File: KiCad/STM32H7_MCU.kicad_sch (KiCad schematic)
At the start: 51 parts, among them IC2 SN74LVC1G14DBVR, IC3 STM32H7R7L8H6H, IC4 TLV75718PDRVR, Y1 VXM7-9032-25M0000000

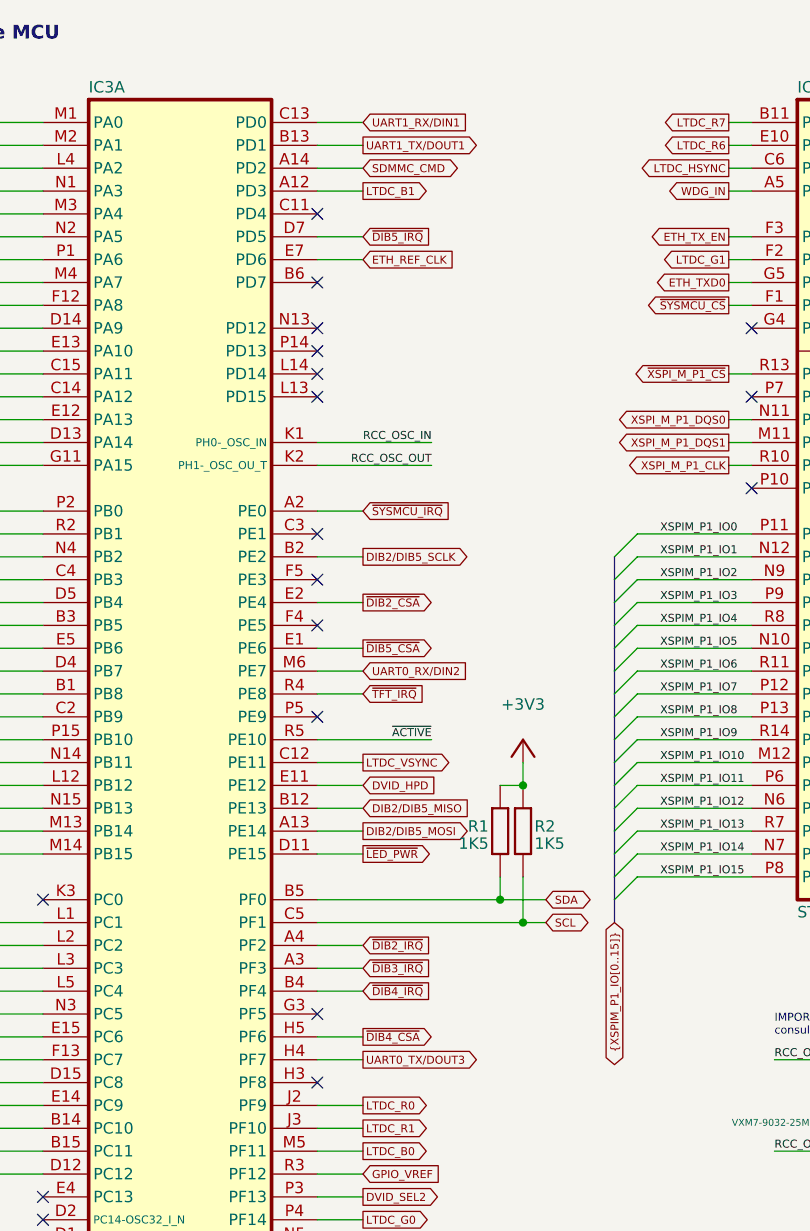
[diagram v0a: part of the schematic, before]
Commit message: DIN3 pin assigned
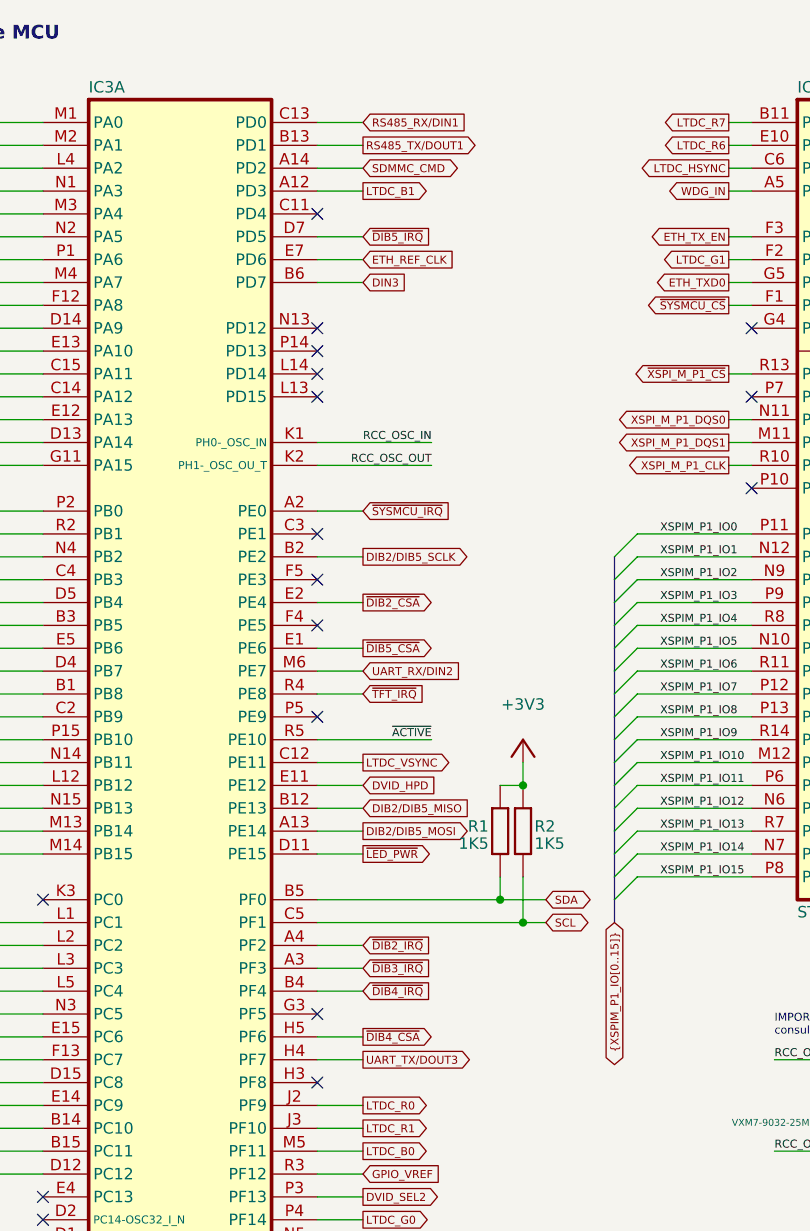
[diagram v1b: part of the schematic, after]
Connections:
- net DIN3: now reaches IC3.B6 (PD7)
- net UART0_RX/DIN2 renamed UART_RX/DIN2
- net UART0_TX/DOUT3 renamed UART_TX/DOUT3
- net UART1_RX/DIN1 renamed RS485_RX/DIN1
- net UART1_TX/DOUT1 renamed RS485_TX/DOUT1
- no-connect marks 27 -> 26
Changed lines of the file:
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@@
 	(title_block
 		(title "${project_name}")
-		(date "2025-11-17")
+		(date "2025-11-23")
 		(rev "${project_version}")
 		(company "${project_creator}")
@@
 	)
 	(no_connect
-		(at 71.12 45.72)
-	)
-	(no_connect
 		(at 71.12 38.1)
 	)
@@
 	(wire
 		(pts
+			(xy 76.2 45.72) (xy 71.12 45.72)
+		)
+		(stroke
+			(width 0)
+			(type default)
+		)
+	)
+	(wire
+		(pts
 			(xy 149.86 137.16) (xy 149.86 139.7)
 		)
@@
 		)
 	)
-	(global_label "UART0_RX{slash}DIN2"
+	(global_label "UART_RX{slash}DIN2"
 		(shape input)
 		(at 76.2 88.9 0)
@@
 		)
 		(property "Intersheetrefs" "${INTERSHEET_REFS}"
-			(at 88.3725 88.9 0)
+			(at 87.5258 88.9 0)
 			(effects
 				(font
@@
 		)
 	)
-	(global_label "UART1_RX{slash}DIN1"
+	(global_label "RS485_RX{slash}DIN1"
 		(shape input)
 		(at 76.2 27.94 0)
@@
 		)
 		(property "Intersheetrefs" "${INTERSHEET_REFS}"
-			(at 88.3725 27.94 0)
+			(at 88.542 27.94 0)
 			(effects
 				(font
@@
 		)
 	)
-	(global_label "UART0_TX{slash}DOUT3"
+	(global_label "UART_TX{slash}DOUT3"
 		(shape output)
 		(at 76.2 132.08 0)
@@
 		)
 		(property "Intersheetrefs" "${INTERSHEET_REFS}"
-			(at 89.3461 132.08 0)
+			(at 88.4994 132.08 0)
 			(effects
 				(font
@@
 		)
 	)
-	(global_label "UART1_TX{slash}DOUT1"
+	(global_label "RS485_TX{slash}DOUT1"
 		(shape output)
 		(at 76.2 30.48 0)
@@
 		)
 		(property "Intersheetrefs" "${INTERSHEET_REFS}"
-			(at 89.3461 30.48 0)
+			(at 89.5156 30.48 0)
 			(effects
 				(font
@@
 				(hide yes)
 			)
+		)
+	)
+	(global_label "DIN3"
+		(shape input)
+		(at 76.2 45.72 0)
+		(fields_autoplaced yes)
+		(effects
+			(font
+				(size 0.889 0.889)
+			)
+			(justify left)
+		)
+		(property "Intersheetrefs" "${INTERSHEET_REFS}"
+			(at 80.9219 45.72 0)
+			(effects
+				(font
+					(size 1.27 1.27)
+				)
+				(justify left)
+				(hide yes)
+			)

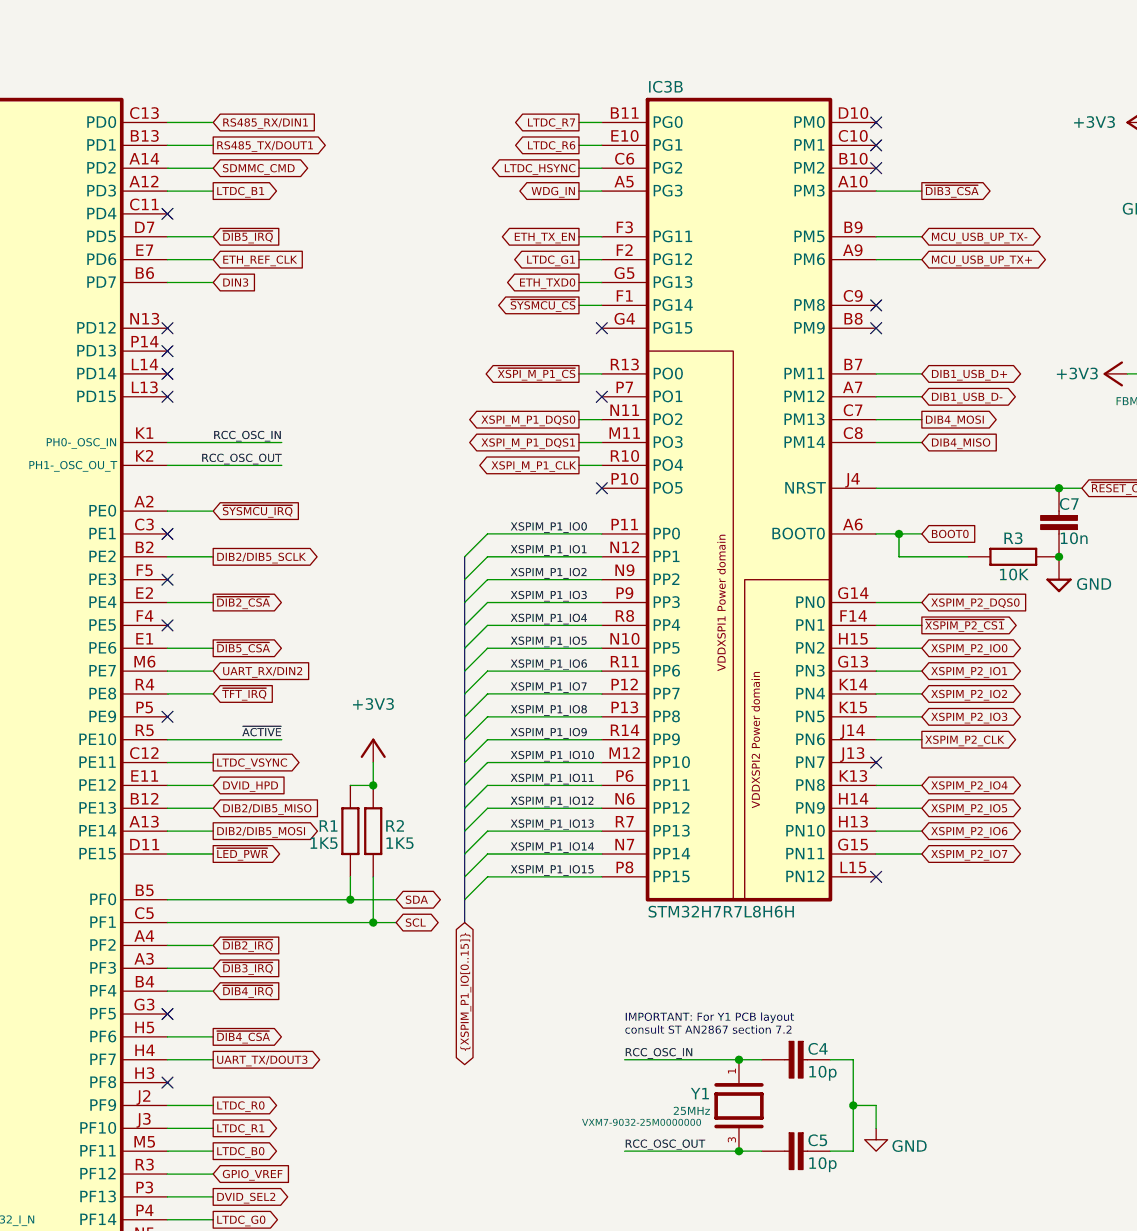
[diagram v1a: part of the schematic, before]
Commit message: ETH clk fixed, digital I/O naming updated
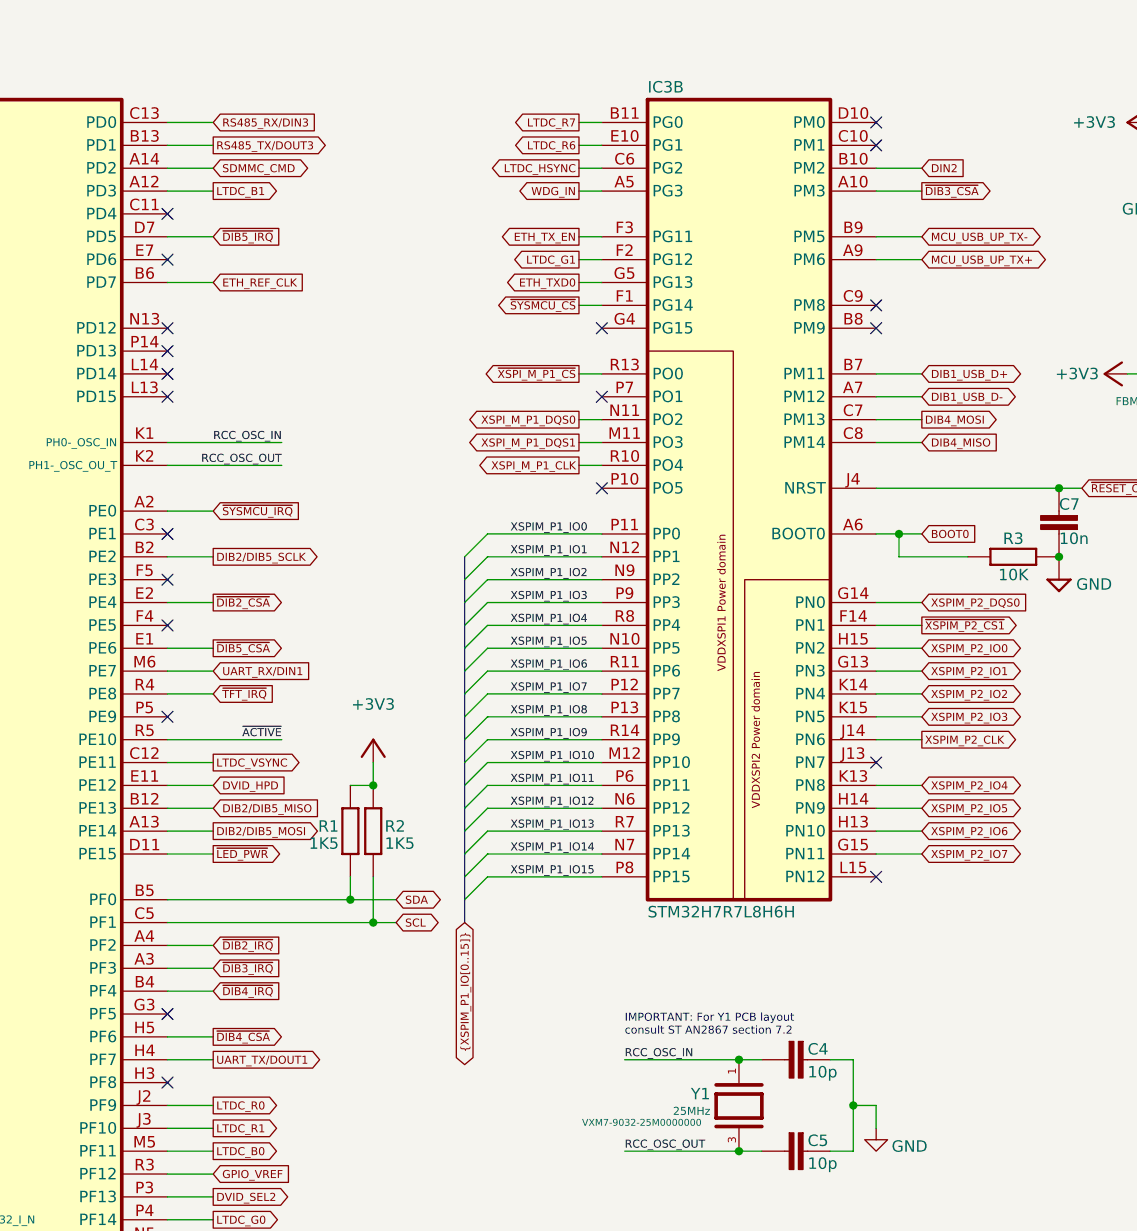
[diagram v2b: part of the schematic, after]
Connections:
- net DIN3 is gone; now on net ETH_REF_CLK: IC3.B6 (PD7)
- net ETH_REF_CLK: no longer IC3.E7 (PD6)
- net DIN2: now reaches IC3.B10 (PM2)
- net RS485_RX/DIN1 renamed RS485_RX/DIN3
- net RS485_TX/DOUT1 renamed RS485_TX/DOUT3
- net UART_RX/DIN2 renamed UART_RX/DIN1
- net UART_TX/DOUT3 renamed UART_TX/DOUT1
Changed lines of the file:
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@@
 	(title_block
 		(title "${project_name}")
-		(date "2025-11-23")
+		(date "2025-11-24")
 		(rev "${project_version}")
 		(company "${project_creator}")
@@
 	)
 	(no_connect
-		(at 149.86 33.02)
+		(at 71.12 73.66)
+	)
+	(no_connect
+		(at 71.12 43.18)
 	)
 	(no_connect
@@
 	)
 	(no_connect
-		(at 71.12 73.66)
-	)
-	(no_connect
 		(at 40.64 149.86)
 	)
@@
 	(wire
 		(pts
-			(xy 76.2 45.72) (xy 71.12 45.72)
-		)
-		(stroke
-			(width 0)
-			(type default)
-		)
-	)
-	(wire
-		(pts
 			(xy 149.86 137.16) (xy 149.86 139.7)
 		)
@@
 	(wire
 		(pts
-			(xy 76.2 43.18) (xy 71.12 43.18)
-		)
-		(stroke
-			(width 0)
-			(type default)
-		)
-	)
-	(wire
-		(pts
 			(xy 149.86 137.16) (xy 147.32 137.16)
 		)
@@
 	(wire
 		(pts
+			(xy 149.86 33.02) (xy 154.94 33.02)
+		)
+		(stroke
+			(width 0)
+			(type default)
+		)
+	)
+	(wire
+		(pts
 			(xy 213.36 40.64) (xy 213.36 43.18)
 		)
@@
 	(wire
 		(pts
+			(xy 76.2 45.72) (xy 71.12 45.72)
+		)
+		(stroke
+			(width 0)
+			(type default)
+		)
+	)
+	(wire
+		(pts
 			(xy 213.36 43.18) (xy 215.9 43.18)
 		)
@@
 		)
 	)
-	(global_label "UART_RX{slash}DIN2"
+	(global_label "UART_RX{slash}DIN1"
 		(shape input)
 		(at 76.2 88.9 0)
@@
 	(global_label "ETH_REF_CLK"
 		(shape input)
-		(at 76.2 43.18 0)
+		(at 76.2 45.72 0)
 		(fields_autoplaced yes)
 		(effects
@@
 		)
 		(property "Intersheetrefs" "${INTERSHEET_REFS}"
-			(at 86.5521 43.18 0)
+			(at 86.5521 45.72 0)
 			(effects
 				(font
@@
 		)
 	)
-	(global_label "RS485_RX{slash}DIN1"
+	(global_label "RS485_RX{slash}DIN3"
 		(shape input)
 		(at 76.2 27.94 0)
@@
 		)
 	)
-	(global_label "UART_TX{slash}DOUT3"
+	(global_label "UART_TX{slash}DOUT1"
 		(shape output)
 		(at 76.2 132.08 0)
@@
 		)
 	)
-	(global_label "RS485_TX{slash}DOUT1"
+	(global_label "RS485_TX{slash}DOUT3"
 		(shape output)
 		(at 76.2 30.48 0)
@@
 		)
 	)
-	(global_label "DIN3"
+	(global_label "DIN2"
 		(shape input)
-		(at 76.2 45.72 0)
+		(at 154.94 33.02 0)
 		(fields_autoplaced yes)
 		(effects
@@
 		)
 		(property "Intersheetrefs" "${INTERSHEET_REFS}"
-			(at 80.9219 45.72 0)
+			(at 159.6619 33.02 0)
 			(effects
 				(font

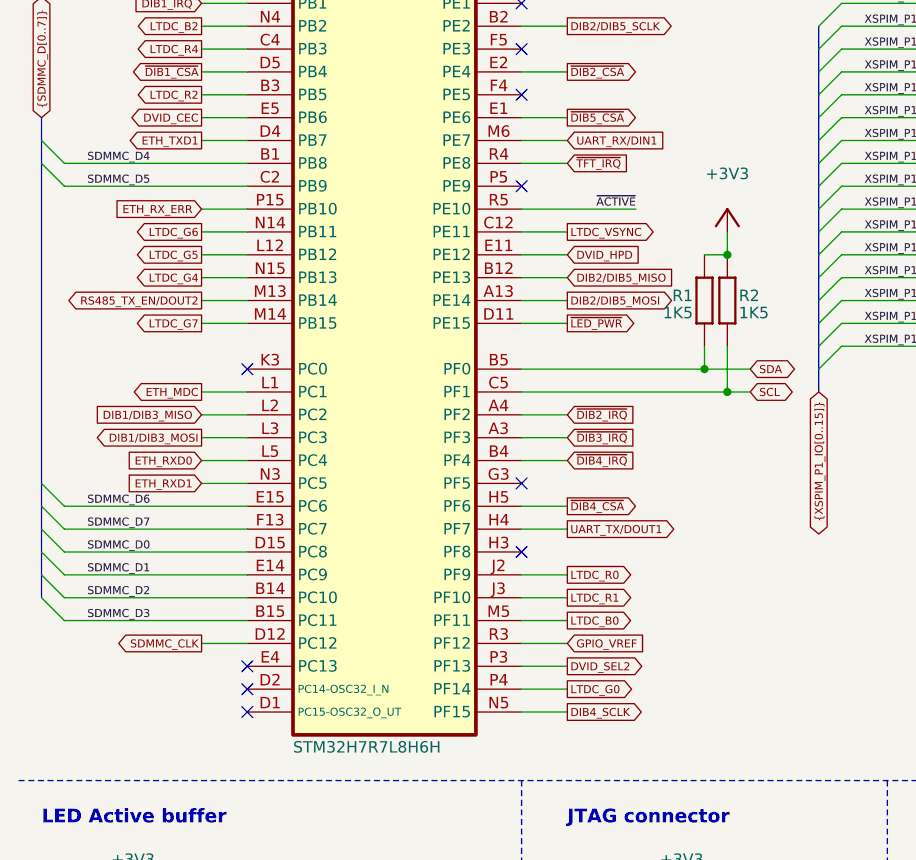
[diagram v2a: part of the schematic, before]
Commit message: RTC input added
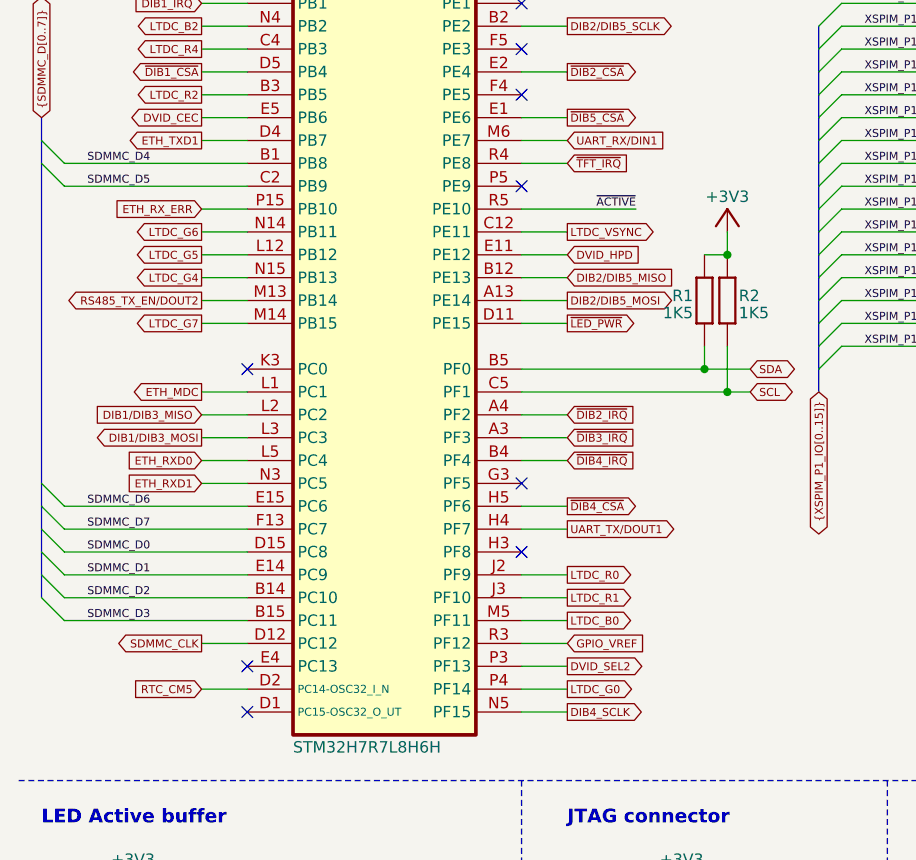
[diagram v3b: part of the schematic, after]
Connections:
- net RTC_CM5: now reaches IC3.D2 (PC14-OSC32_I_N)
- no-connect marks 26 -> 25
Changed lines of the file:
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@@
 	(title_block
 		(title "${project_name}")
-		(date "2025-11-24")
+		(date "2025-11-28")
 		(rev "${project_version}")
 		(company "${project_creator}")
@@
 	)
 	(no_connect
-		(at 40.64 149.86)
-	)
-	(no_connect
 		(at 71.12 58.42)
 	)
@@
 	(wire
 		(pts
+			(xy 35.56 149.86) (xy 40.64 149.86)
+		)
+		(stroke
+			(width 0)
+			(type default)
+		)
+	)
+	(wire
+		(pts
 			(xy 154.94 101.6) (xy 149.86 101.6)
 		)
@@
 		)
 	)
+	(global_label "RTC_CM5"
+		(shape input)
+		(at 35.56 149.86 180)
+		(fields_autoplaced yes)
+		(effects
+			(font
+				(size 0.889 0.889)
+			)
+			(justify right)
+		)
+		(property "Intersheetrefs" "${INTERSHEET_REFS}"
+			(at 28.0441 149.86 0)
+			(effects
+				(font
+					(size 1.27 1.27)
+				)
+				(justify right)
+				(hide yes)
+			)
+		)
+	)
 	(global_label "LTDC_R0"
 		(shape output)
@@
 		)
 		(property "Value" "+3V3"
-			(at 93.98 93.345 0)
+			(at 93.98 95.885 0)
 			(effects
 				(font
